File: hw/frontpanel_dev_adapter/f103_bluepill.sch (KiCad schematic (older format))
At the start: 42 parts, among them J501 Conn_01x20, J502 Conn_01x20, J503 SWD, J504 STX-3501-3N_(TTL-232R-xV-AJ), Q501 AO3401A, SW501 SKHUxxE010, U501 STM32F103CBTx, U502 W25Q64FV, U503 CAT24C256, U504 DS3231MZ, Y501 8.0M

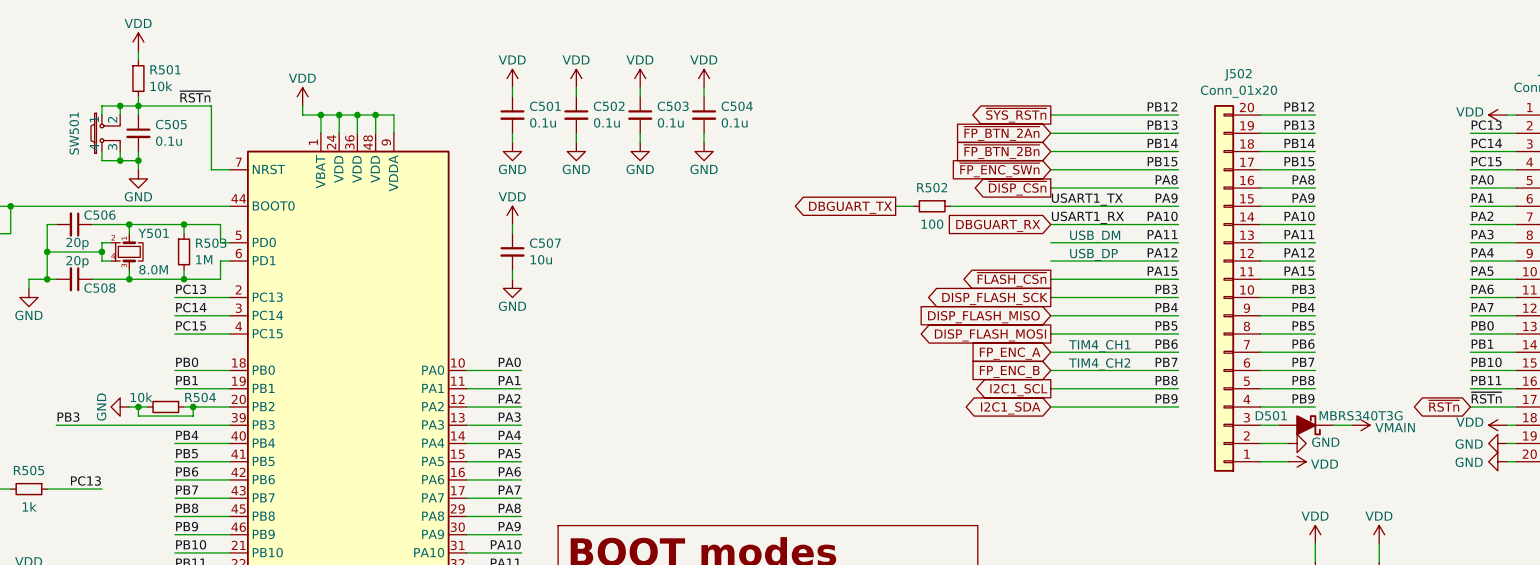
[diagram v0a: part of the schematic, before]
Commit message: "Frontpanel dev-adapter: change some component sizes, add Logo & 4x mounting holes"
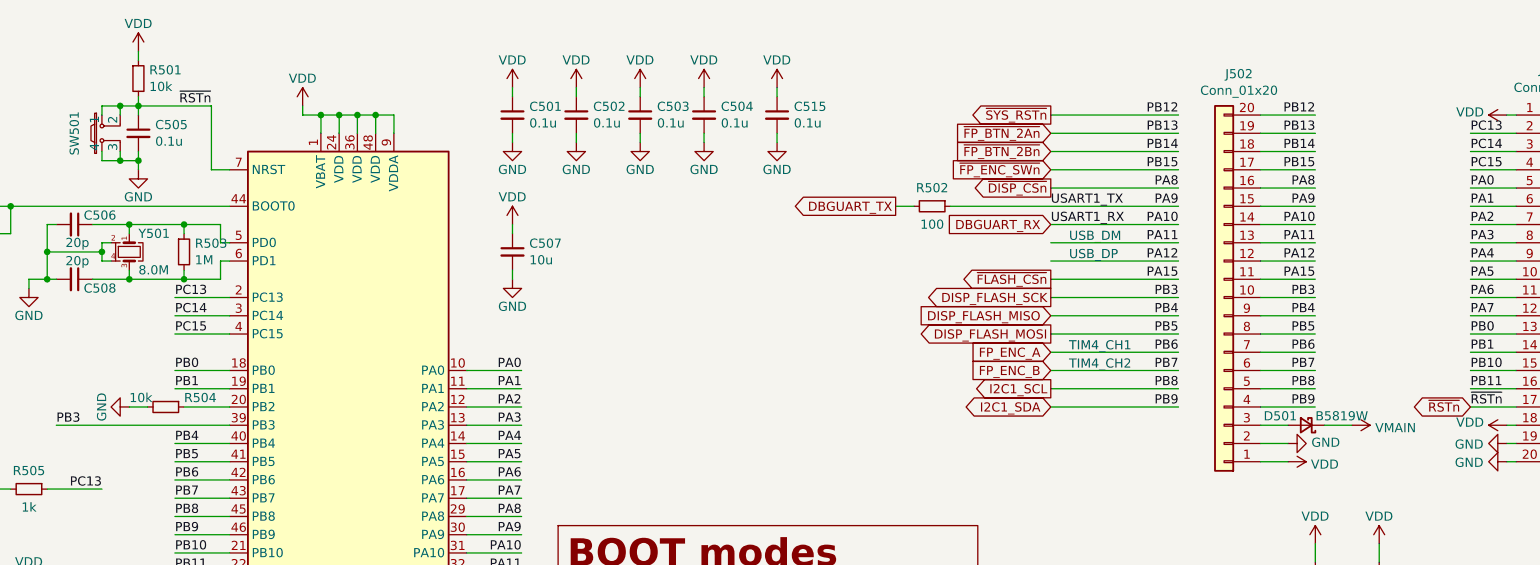
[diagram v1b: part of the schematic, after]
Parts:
- removed D501: MBRS340T3G, customlib_mj_fp:MBRS3xx_SMC_CASE_403AC, symbol customlib_mj:MBRS340T3G
- added C515: 0.1u, Capacitor_SMD:C_0402_1005Metric, symbol Device:C_Small
- added D501: B5819W, Diode_SMD:D_SOD-123, symbol customlib_mj:B5819W
- C501, C502, C503, C504: footprint Capacitor_SMD:C_0603_1608Metric -> Capacitor_SMD:C_0402_1005Metric
- JP501: footprint customlib_mj_fp:db2_ud_0603 -> customlib_mj_fp:db3_ud_0603
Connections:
- net GND: now also C515.2; no longer R504.1, U501.20 (PB2)
- net VDD: now also C515.1
- net VMAIN: now also D501.1 (K)
- net at J502.3 (Pin_3): now also D501.2 (A)
- new net: R504.1, U501.20 (PB2)
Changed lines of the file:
@@
 F 0 "C501" H 3992 1146 50  0000 L CNN
 F 1 "0.1u" H 3992 1055 50  0000 L CNN
-F 2 "Capacitor_SMD:C_0603_1608Metric" H 3900 1100 50  0001 C CNN
+F 2 "Capacitor_SMD:C_0402_1005Metric" H 3900 1100 50  0001 C CNN
 F 3 "~" H 3900 1100 50  0001 C CNN
 	1    3900 1100
@@
 F 0 "C502" H 4342 1146 50  0000 L CNN
 F 1 "0.1u" H 4342 1055 50  0000 L CNN
-F 2 "Capacitor_SMD:C_0603_1608Metric" H 4250 1100 50  0001 C CNN
+F 2 "Capacitor_SMD:C_0402_1005Metric" H 4250 1100 50  0001 C CNN
 F 3 "~" H 4250 1100 50  0001 C CNN
 	1    4250 1100
@@
 F 0 "C503" H 4692 1146 50  0000 L CNN
 F 1 "0.1u" H 4692 1055 50  0000 L CNN
-F 2 "Capacitor_SMD:C_0603_1608Metric" H 4600 1100 50  0001 C CNN
+F 2 "Capacitor_SMD:C_0402_1005Metric" H 4600 1100 50  0001 C CNN
 F 3 "~" H 4600 1100 50  0001 C CNN
 	1    4600 1100
@@
 F 0 "C504" H 5042 1146 50  0000 L CNN
 F 1 "0.1u" H 5042 1055 50  0000 L CNN
-F 2 "Capacitor_SMD:C_0603_1608Metric" H 4950 1100 50  0001 C CNN
+F 2 "Capacitor_SMD:C_0402_1005Metric" H 4950 1100 50  0001 C CNN
 F 3 "~" H 4950 1100 50  0001 C CNN
 	1    4950 1100
@@
 	0    1    1    0
 $EndComp
-Wire Wire Line
-	2100 2700 2150 2700
-Wire Wire Line
-	1900 2700 1850 2700
-Wire Wire Line
-	2150 2700 2150 2750
-Wire Wire Line
-	1850 2750 1850 2700
-Connection ~ 2150 2700
-Connection ~ 1850 2700
-Wire Wire Line
-	1850 2700 1800 2700
 $Comp
 L customlib_mj:dogbone_3_ud JP501
@@
 F 0 "JP501" V 950 1756 50  0000 C CNN
 F 1 "dogbone_3_ud" H 975 1750 50  0001 C CNN
-F 2 "customlib_mj_fp:db2_ud_0603" H 950 1600 50  0001 C CNN
+F 2 "customlib_mj_fp:db3_ud_0603" H 950 1600 50  0001 C CNN
 F 3 "" H 950 1600 50  0001 C CNN
 	1    950  1600
@@
 Wire Wire Line
 	1150 1600 2350 1600
-$Comp
-L customlib_mj:MBRS340T3G D501
-U 1 1 6011E6C4
-P 8250 2800
-F 0 "D501" H 8350 2750 50  0000 L CNN
-F 1 "MBRS340T3G" H 7950 2750 50  0000 C CNN
-F 2 "customlib_mj_fp:MBRS3xx_SMC_CASE_403AC" H 8250 2625 50  0001 C CNN
-F 3 "https://www.onsemi.com/pub/Collateral/MBRS340T3-D.PDF" H 8250 2800 50  0001 C CNN
-	1    8250 2800
-	-1   0    0    1
-$EndComp
 $Comp
 L customlib_mj:STM32_bootmodes #TXT0501
@@
 Wire Wire Line
 	2350 2600 2050 2600
-Wire Wire Line
-	2150 2700 2350 2700
 Wire Wire Line
 	2350 2800 1400 2800
@@
 SWCLK
 Wire Wire Line
-	8000 2800 8100 2800
-Wire Wire Line
-	8400 2800 8500 2800
+	8000 2800 8150 2800
+Wire Wire Line
+	8350 2800 8500 2800
 Wire Wire Line
 	1400 1700 1350 1700
@@
 	3150 6200 3150 6250
 Wire Wire Line
-	1850 2750 2150 2750
+	1800 2700 1900 2700
+Wire Wire Line
+	2100 2700 2350 2700
+$Comp
+L Device:C_Small C515
+U 1 1 5FE9BE20
+P 5350 1100
+F 0 "C515" H 5442 1146 50  0000 L CNN
+F 1 "0.1u" H 5442 1055 50  0000 L CNN
+F 2 "Capacitor_SMD:C_0402_1005Metric" H 5350 1100 50  0001 C CNN
+F 3 "~" H 5350 1100 50  0001 C CNN
+	1    5350 1100
+	1    0    0    -1
+$EndComp
+$Comp
+L power:GND #PWR0562
+U 1 1 5FE9C63E
+P 5350 1250
+F 0 "#PWR0562" H 5350 1000 50  0001 C CNN
+F 1 "GND" H 5350 1100 50  0000 C CNN
+F 2 "" H 5350 1250 50  0001 C CNN
+F 3 "" H 5350 1250 50  0001 C CNN
+	1    5350 1250
+	1    0    0    -1
+$EndComp
+Wire Wire Line
+	5350 1250 5350 1200
+$Comp
+L power:VDD #PWR0561
+U 1 1 5FE9C649
+P 5350 950
+F 0 "#PWR0561" H 5350 800 50  0001 C CNN
+F 1 "VDD" H 5350 1100 50  0000 C CNN
+F 2 "" H 5350 950 50  0001 C CNN
+F 3 "" H 5350 950 50  0001 C CNN
+	1    5350 950
+	1    0    0    -1
+$EndComp
+Wire Wire Line
+	5350 950  5350 1000
+$Comp
+L customlib_mj:B5819W D501
+U 1 1 5FE29537
+P 8250 2800
+F 0 "D501" H 8300 2750 50  0000 L CNN
+F 1 "B5819W" H 8200 2750 50  0000 R CNN
+F 2 "Diode_SMD:D_SOD-123" V 8250 2800 50  0001 C CNN
+F 3 "https://datasheet.lcsc.com/szlcsc/Changjiang-Electronics-Tech-CJ-B5819W_C8598.pdf" V 8250 2800 50  0001 C CNN
+	1    8250 2800
+	-1   0    0    1
+$EndComp
 $EndSCHEMATC

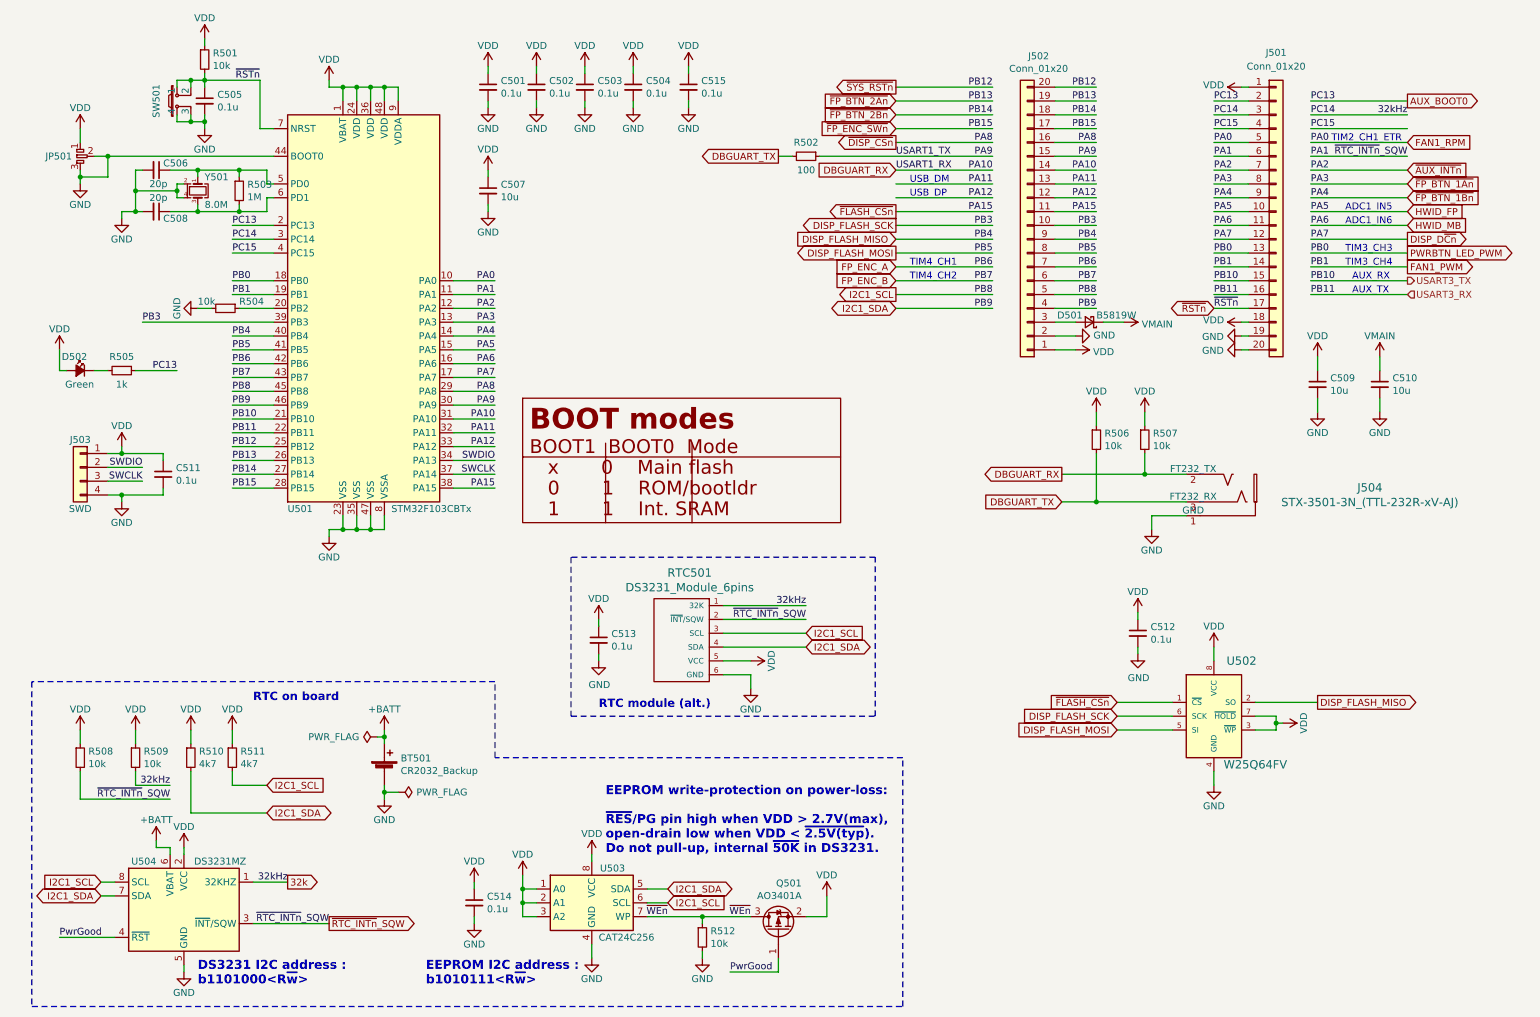
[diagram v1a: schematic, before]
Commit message: Frontpanel dev adapter: Optimize some LCSC components for JLC assembly; add some datasheets. Optimize F103 16MHz xtal routing
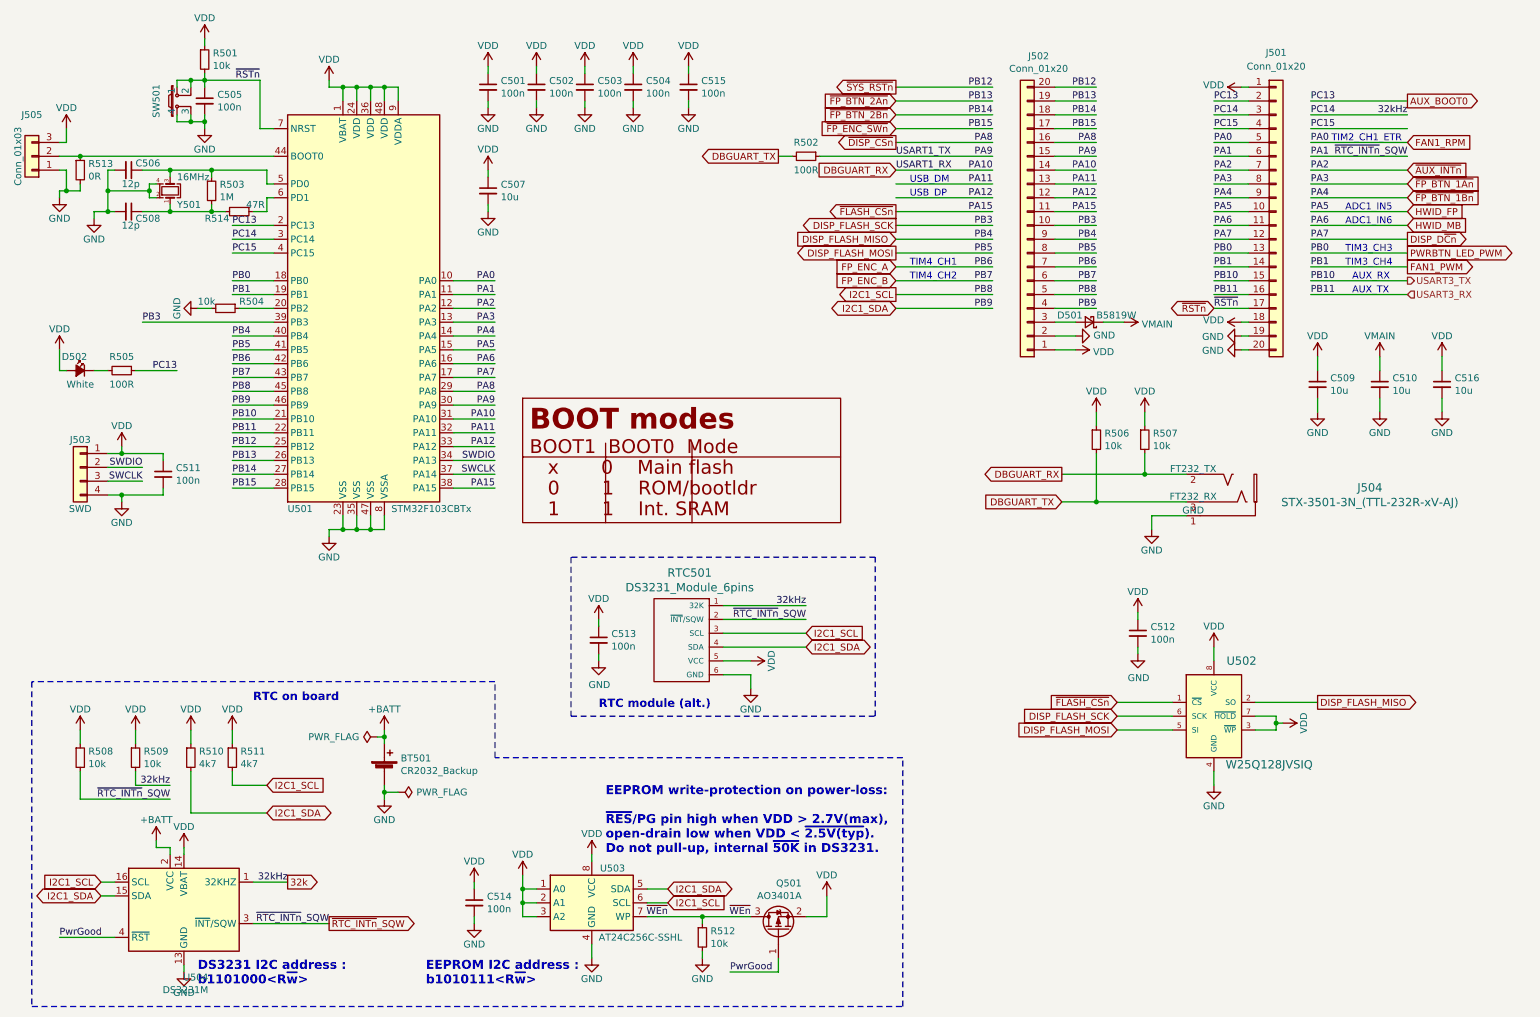
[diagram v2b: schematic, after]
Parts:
- removed JP501: dogbone_3_ud, customlib_mj_fp:db3_ud_0603, symbol customlib_mj:dogbone_3_ud
- removed U504: DS3231MZ, Package_SO:SOIC-8_3.9x4.9mm_P1.27mm, symbol Timer_RTC:DS3231MZ
- added C516: 10u, Capacitor_SMD:C_0603_1608Metric, symbol Device:C_Small
- added J505: Conn_01x03, Connector_PinHeader_2.54mm:PinHeader_1x03_P2.54mm_Vertical, symbol Connector_Generic:Conn_01x03
- added R513: 0R, Resistor_SMD:R_0402_1005Metric, symbol Device:R_Small
- added R514: 47R, Resistor_SMD:R_0402_1005Metric, symbol Device:R_Small
- added U504: DS3231M, Package_SO:SOIC-16W_7.5x10.3mm_P1.27mm, symbol Timer_RTC:DS3231M
- C501, C502, C503, C504, C515: value 0.1u -> 100n
- C505, C511, C512, C513, C514: value 0.1u -> 100n; footprint Capacitor_SMD:C_0603_1608Metric -> Capacitor_SMD:C_0402_1005Metric
- C506, C508: value 20p -> 12p; footprint Capacitor_SMD:C_0603_1608Metric -> Capacitor_SMD:C_0402_1005Metric
- D502: value Green -> White
- R501, R503, R504, R506, R507, R508, R509, R510, R511, R512: footprint Resistor_SMD:R_0603_1608Metric -> Resistor_SMD:R_0402_1005Metric
- R502: value 100 -> 100R; footprint Resistor_SMD:R_0603_1608Metric -> Resistor_SMD:R_0402_1005Metric
- R505: value 1k -> 100R; footprint Resistor_SMD:R_0603_1608Metric -> Resistor_SMD:R_0402_1005Metric
- U502: value W25Q64FV -> W25Q128JVSIQ
- U503: value CAT24C256 -> AT24C256C-SSHL
- Y501: value 8.0M -> 16MHz
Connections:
- net +BATT: now also U504.2 (VCC)
- net 32k: now also U504.1 (32KHZ)
- net GND: now also C516.2, J505.1 (Pin_1), R513.2, U504.10 (GND), U504.11 (GND), U504.12 (GND), U504.13 (GND), U504.5 (GND), U504.6 (GND), U504.7 (GND), U504.8 (GND), U504.9 (GND); no longer U501.44 (BOOT0)
- net I2C1_SCL: now also U504.16 (SCL)
- net I2C1_SDA: now also U504.15 (SDA)
- net PwrGood: now also U504.4 (~RST)
- net VDD: now also C516.1, J505.3 (Pin_3), U504.14 (VBAT)
- net ~RTC_INTn~_SQW: now also U504.3 (~INT~/SQW)
- net at C506.1, R503.1, U501.5 (PD0): now also Y501.3; no longer Y501.1
- net at C508.1, R503.2: now also Y501.1, R514.2; no longer U501.6 (PD1), Y501.3
- new net: J505.2 (Pin_2), R513.1, U501.44 (BOOT0)
- new net: R514.1, U501.6 (PD1)
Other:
- moved on the sheet: C506, C508, R503, Y501
